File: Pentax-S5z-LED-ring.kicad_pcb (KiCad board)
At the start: 2 copper layers, 40 x 40 mm, 52 parts, among them IC1 ATTINY13-S, P1 CONN_2, P2 +, P3 -, P4 CONN_2, Q1 MOSFET_N, SW1 SW_PUSH, SW2 SW_PUSH

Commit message: Minute tweaks.
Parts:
- P2: value + -> A
- P3: value - -> B
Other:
- board text added: "A"
- board text added: "B"
- board text removed: "A+"
- board text removed: "B-"
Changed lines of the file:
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@@
-(kicad_pcb (version 3) (host pcbnew "(2013-05-08 BZR 4145)-testing")
+(kicad_pcb (version 3) (host pcbnew "(2013-09-20 BZR 4325)-product")
   (general
     (links 71)
     (no_connects 0)
-    (area 37.066667 44.422948 92.483333 85.577052)
+    (area 37.066667 44.949999 92.483333 85.050001)
     (thickness 1.6)
     (drawings 26)
@@
     (mod_text_size 1 1)
     (mod_text_width 0.2)
-    (pad_size 1.5 1.4)
+    (pad_size 1.5 1.2)
     (pad_drill 0)
     (pad_to_mask_clearance 0)
@@
     (visible_elements FFFFFF7F)
     (pcbplotparams
-      (layerselection 300974081)
+      (layerselection 284196865)
       (usegerberextensions true)
       (excludeedgelayer true)
-      (linewidth 152400)
+      (linewidth 0.150000)
       (plotframeref false)
       (viasonmask false)
@@
       (effects (font (size 1 1) (thickness 0.2)) (justify mirror))
     )
-    (fp_text value + (at -2.75 0) (layer B.SilkS)
+    (fp_text value A (at -2.35 0.05) (layer B.SilkS)
       (effects (font (size 1 1) (thickness 0.2)) (justify mirror))
     )
@@
       (effects (font (size 1 1) (thickness 0.2)) (justify mirror))
     )
-    (fp_text value - (at 2.5 0) (layer B.SilkS)
+    (fp_text value B (at 2.25 0.05) (layer B.SilkS)
       (effects (font (size 1 1) (thickness 0.2)) (justify mirror))
     )
@@
     (fp_line (start -3 1.85) (end -3 -1.85) (layer F.SilkS) (width 0.2))
     (fp_line (start -3 -1.85) (end 3 -1.85) (layer F.SilkS) (width 0.2))
-    (pad 1 smd rect (at -3.9 0 205) (size 1.5 1.4)
+    (pad 1 smd rect (at -3.9 0 205) (size 1.5 1.2)
       (layers F.Cu F.Mask)
       (net 7 N-0000011)
@@
     (fp_line (start -3 1.85) (end -3 -1.85) (layer F.SilkS) (width 0.2))
     (fp_line (start -3 -1.85) (end 3 -1.85) (layer F.SilkS) (width 0.2))
-    (pad 1 smd rect (at -3.9 0 335) (size 1.5 1.4)
+    (pad 1 smd rect (at -3.9 0 335) (size 1.5 1.2)
       (layers F.Cu F.Mask)
       (net 15 N-000002)
@@
     (effects (font (size 1 1) (thickness 0.2)))
   )
-  (gr_text B- (at 55.6 61.2 90) (layer F.SilkS)
+  (gr_text B (at 55.6 61.6 90) (layer F.SilkS)
     (effects (font (size 1 1) (thickness 0.2)))
   )
-  (gr_text A+ (at 55.6 68.7 90) (layer F.SilkS)
+  (gr_text A (at 55.6 68.4 90) (layer F.SilkS)
     (effects (font (size 1 1) (thickness 0.2)))
   )

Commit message: Added 3D modules for the PLCC2-3528 LEDs + silkscreen tweaks.
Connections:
- IC1 pad 2: N-000006 -> (no net)
- IC1 pad 3: N-000005 -> (no net)
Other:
- board text added: "+"

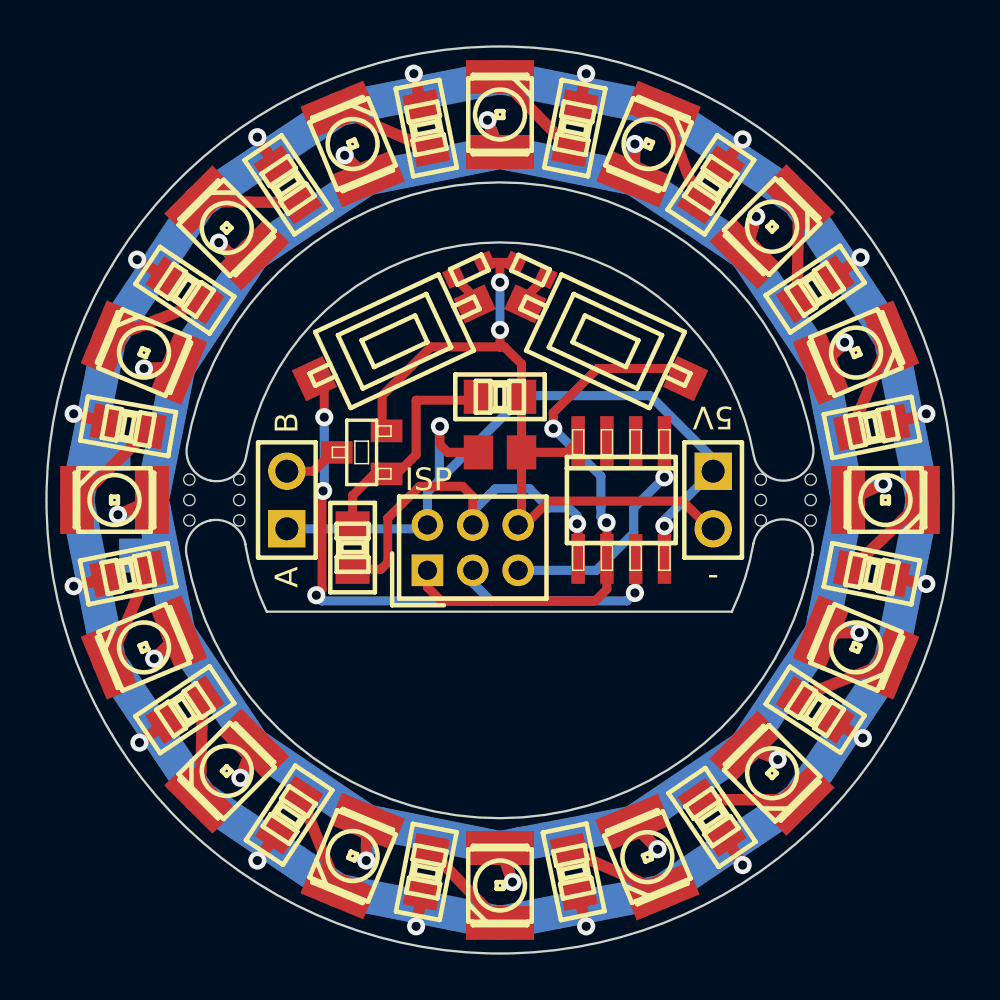
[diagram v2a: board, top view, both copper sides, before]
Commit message: Switched ATtiny13 to DFN10 package.
Had to move to KiCAD's new way of handling footprint libraries.
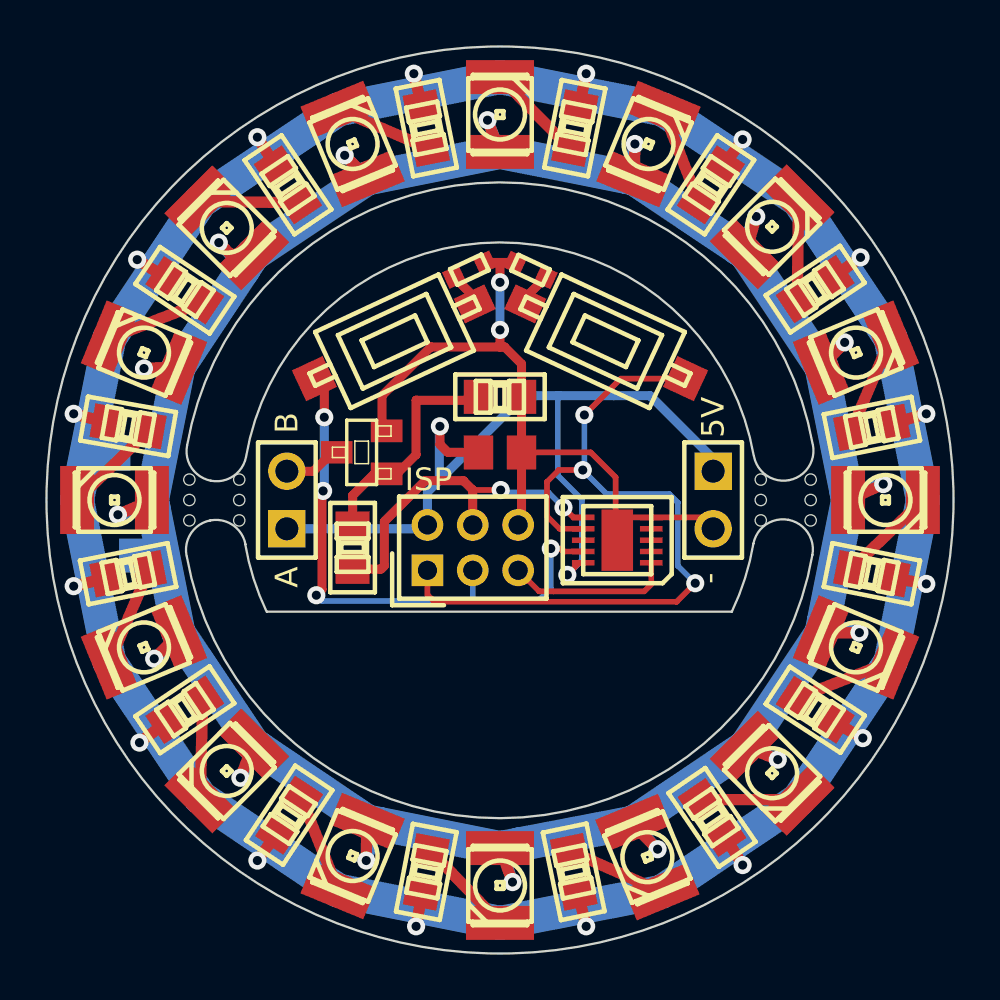
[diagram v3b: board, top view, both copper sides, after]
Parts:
- IC1: value ATTINY13-S -> MADW__ATTINY13-MM; footprint -SOIC8 -> my_parts:MADW__MLF10
- P2: value A -> +
- P3: value B -> -
- moved IC1 1.78 mm to (70.2, 66.8)
- moved G2 1.38 mm to (71.1, 63.1)
- moved G1 0.77 mm to (59.1, 63.2)
- renumbered G*** to G1, G*** to G1.1, G*** to G2, G*** to G2.1
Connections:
- IC1 pad 2: (no net) -> Net-(IC1-Pad2)
- IC1 pad 3: (no net) -> Net-(IC1-Pad3)
- IC1 pad 4: GND -> Net-(IC1-Pad4)
- IC1 pad 5: /PWM -> GND
- IC1 pad 6: /MISO -> /PWM
- IC1 pad 7: /SCK -> /MISO
- IC1 pad 8: +5V -> Net-(IC1-Pad8)
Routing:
- net /MISO: track 24.6 -> 34.8 mm, vias 2 -> 3
- net +5V: track 34.1 -> 38.9 mm
- net /RESET: track 10.4 -> 7.33 mm, vias 1 -> 0
- net /PWM: track 17.4 -> 15.1 mm, vias 1 -> 2
- net /SCK: track 27.4 -> 25.4 mm
- net Net-(D1-Pad1): track 152.8 -> 151.0 mm
- net GND: track 33.9 -> 35.1 mm
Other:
- net class Default: clearance 0.25 -> 0.2
- rule trace_clearance: 0.25 -> 0.2
- board text added: "V1.01.a"
- board text added: "V1.01.a 2013"
- board text removed: "+"
- board text removed: "V1.0"
- board text removed: "V1.0 2013"

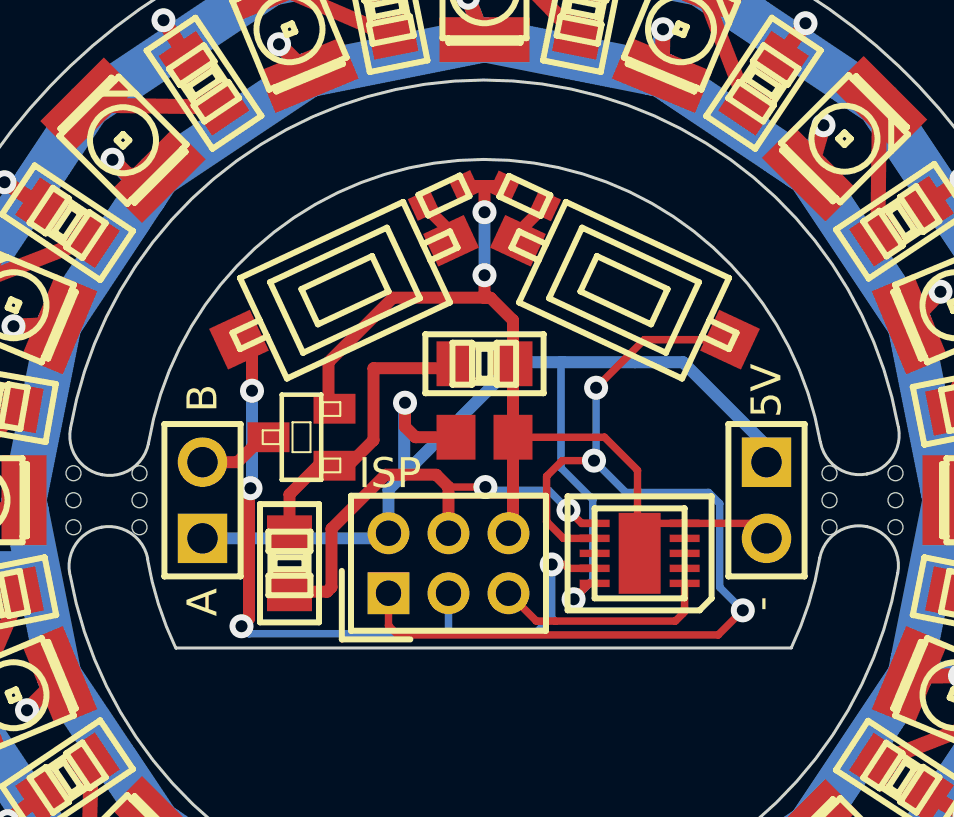
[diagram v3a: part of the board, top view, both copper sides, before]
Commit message: Shoved some traces around to stay clear of button switch bodies.
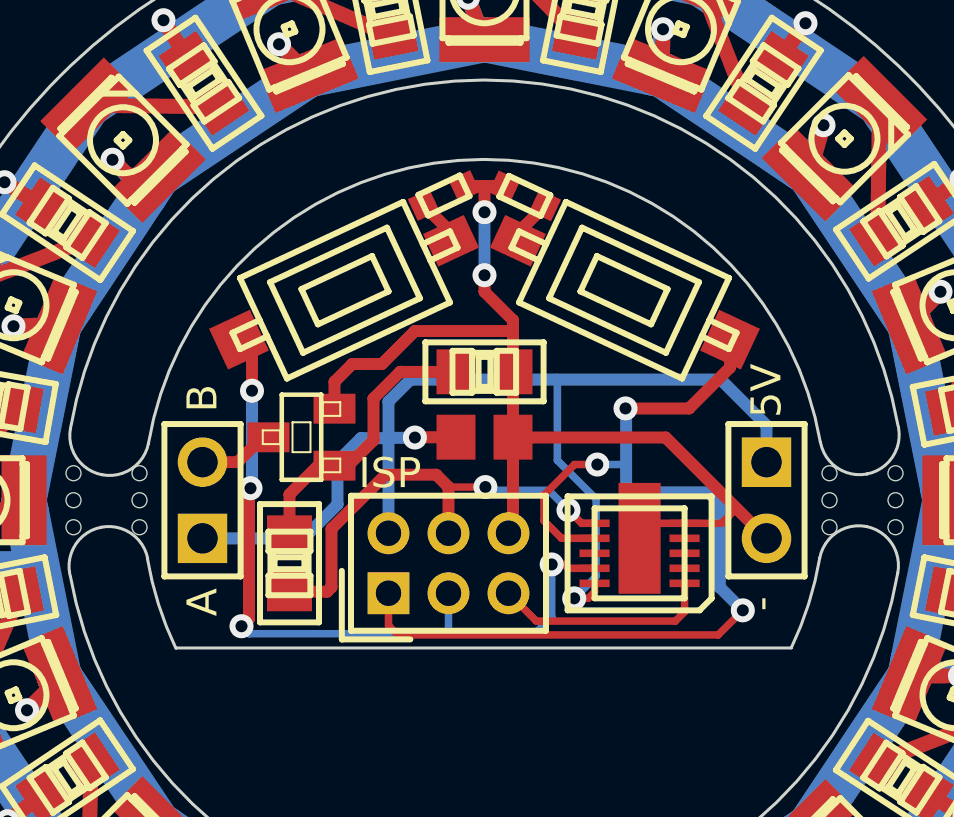
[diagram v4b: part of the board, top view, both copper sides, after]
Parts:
- moved R18 0.27 mm to (65.0, 60.7)
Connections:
- IC1 pad 2: Net-(IC1-Pad2) -> (no net)
- IC1 pad 3: Net-(IC1-Pad3) -> (no net)
- IC1 pad 4: Net-(IC1-Pad4) -> (no net)
- IC1 pad 8: Net-(IC1-Pad8) -> (no net)
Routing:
- net GND: track 35.1 -> 36.0 mm
- net Net-(Q1-Pad1): track 10.1 -> 9.40 mm

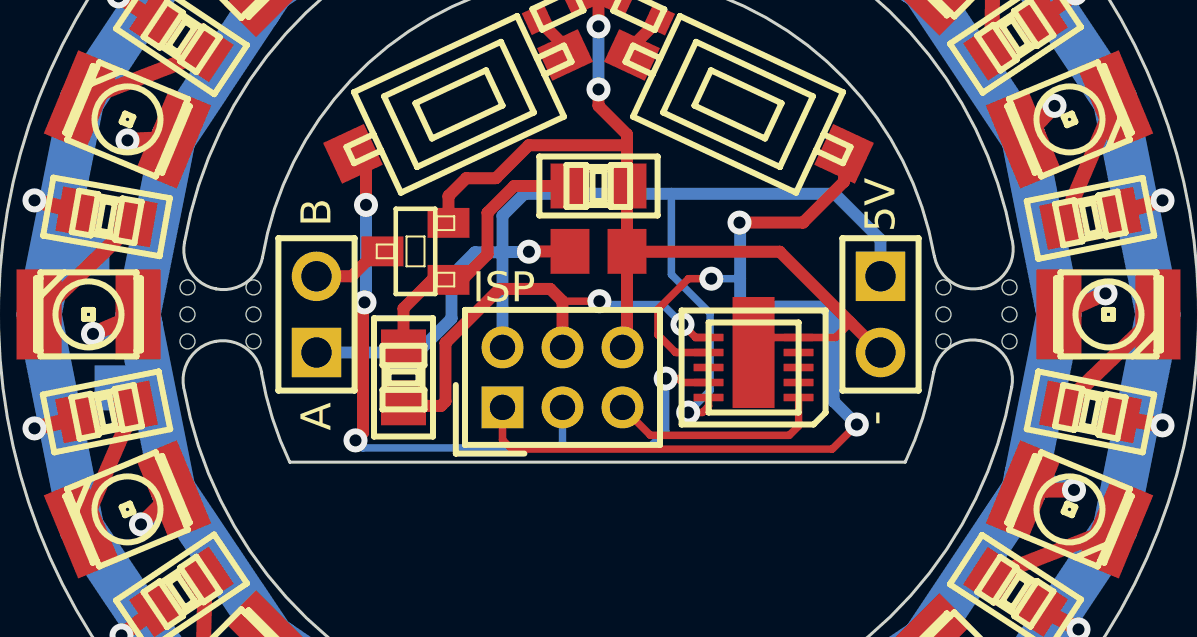
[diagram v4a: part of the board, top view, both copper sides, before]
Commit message: Replaced ISP-header with a pogo-pin compatible one (1.27mm pin-spacing).
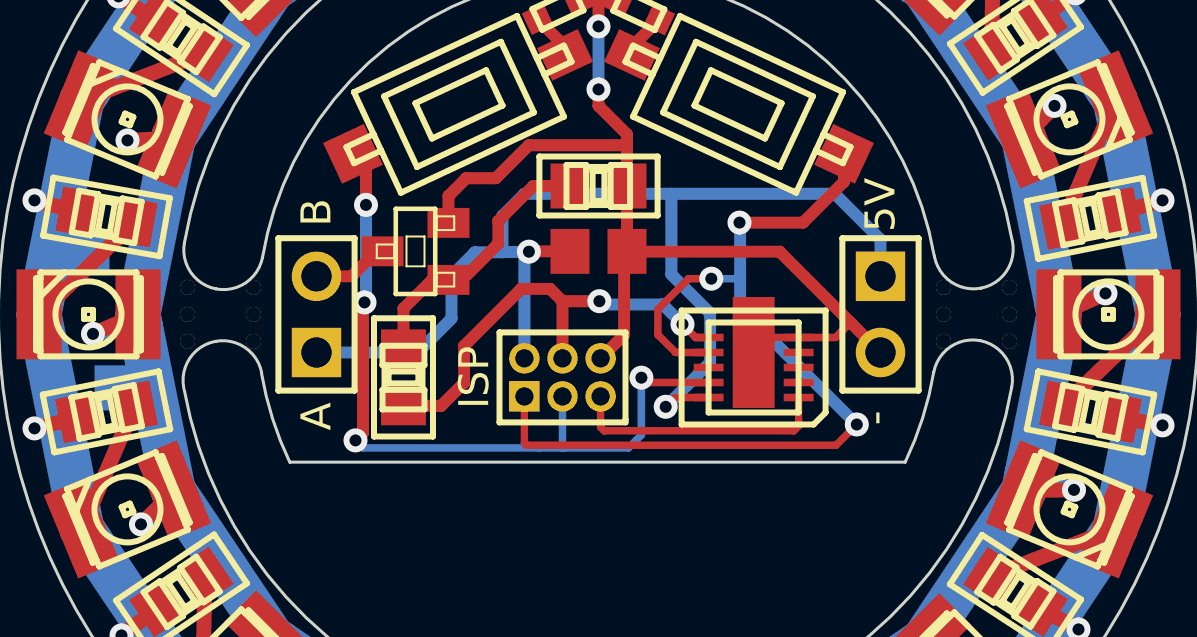
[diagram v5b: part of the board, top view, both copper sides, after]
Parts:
- JP1: footprint MADW__PIN_ARRAY_3x2_2mm -> my_parts:MADW__PIN_ARRAY_3x2_1.27mm
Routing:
- net /MISO: track 34.4 -> 32.3 mm
- net /RESET: track 7.33 -> 8.69 mm
- net +5V: track 39.1 -> 40.1 mm
- net GND: track 36.0 -> 36.6 mm
- net /SCK: track 25.2 -> 25.7 mm
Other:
- board text added: "V1.01.b"
- board text added: "V1.01.b 2013"
- board text removed: "V1.01.a"
- board text removed: "V1.01.a 2013"

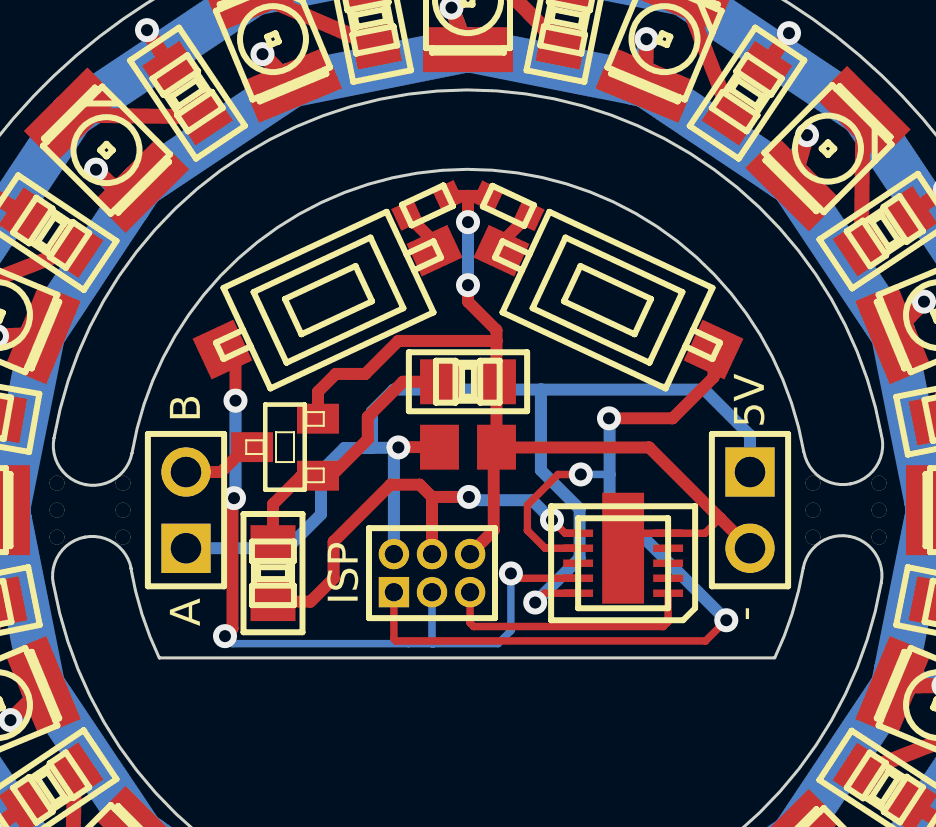
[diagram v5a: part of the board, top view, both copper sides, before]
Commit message: Shoved some parts around. Should be a bit easier to assemble.
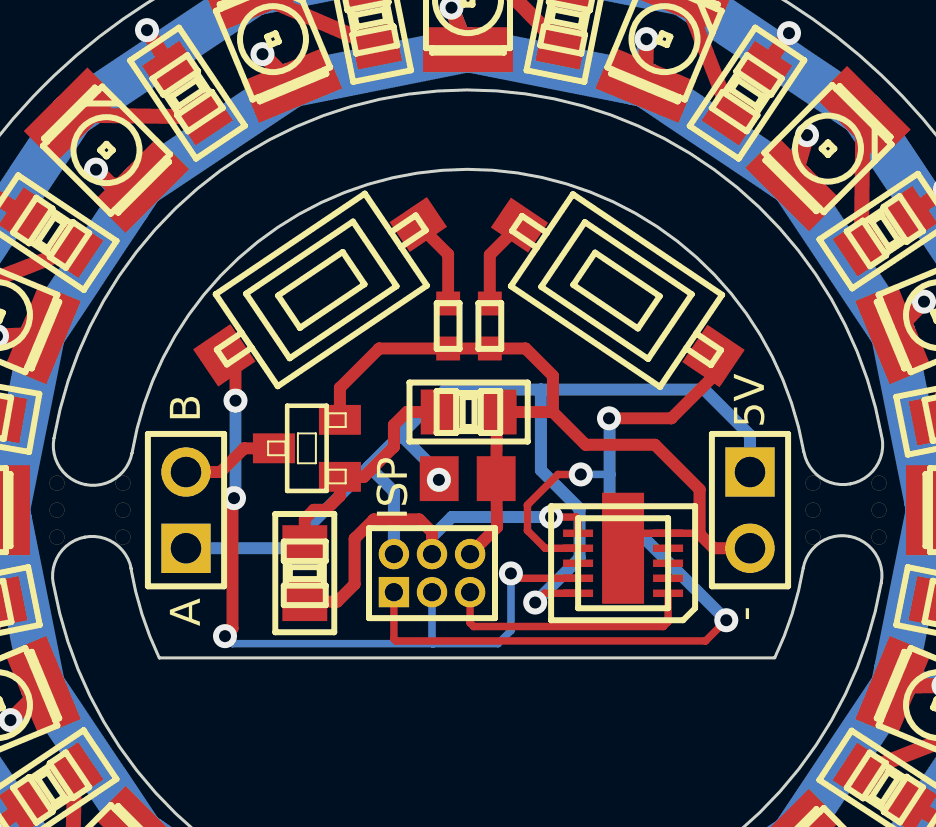
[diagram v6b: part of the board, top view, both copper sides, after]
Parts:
- moved R20 4.07 mm to (64.3, 58.9), turned to 270 degrees
- moved R19 4.06 mm to (65.7, 58.9), turned to 270 degrees
- moved R17 1.06 mm to (59.6, 67.1)
- moved C1 1.05 mm to (65.0, 64.0)
- moved R18 1.01 mm to (65.0, 61.7)
- moved Q1 0.73 mm to (59.6, 62.9)
- moved SW1 0.44 mm to (70.0, 57.7), turned to 326 degrees
- moved SW2 0.42 mm to (60.1, 57.7), turned to 214 degrees
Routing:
- net GND: track 36.6 -> 30.7 mm, vias 2 -> 0
- net +5V: track 40.1 -> 38.0 mm
- net /PWM: track 15.1 -> 13.4 mm, vias 2 -> 1
- net Net-(R20-Pad1): track 1.57 -> 3.05 mm
- net Net-(R19-Pad1): track 1.56 -> 3.02 mm
- net Net-(Q1-Pad1): track 9.03 -> 7.65 mm
- net Net-(P4-Pad2): track 2.34 -> 3.26 mm
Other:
- board text added: "V1.01.c"
- board text added: "V1.01.c 2013"
- board text removed: "V1.01.b"
- board text removed: "V1.01.b 2013"

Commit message: Layout tweaks.
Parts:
- C1: footprint MADW__C0805 -> my_parts:MADW__C0805
- moved R18 0.23 mm to (65.0, 61.5)
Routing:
- net /MISO: track 32.0 -> 31.0 mm
- net /SCK: track 25.5 -> 24.8 mm
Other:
- board text added: "+"
- board text added: "IN"
- board text added: "OUT"
- board text added: "V1.01.d"
- board text added: "V1.01.d 2013"
- board text removed: "V1.01.c"
- board text removed: "V1.01.c 2013"

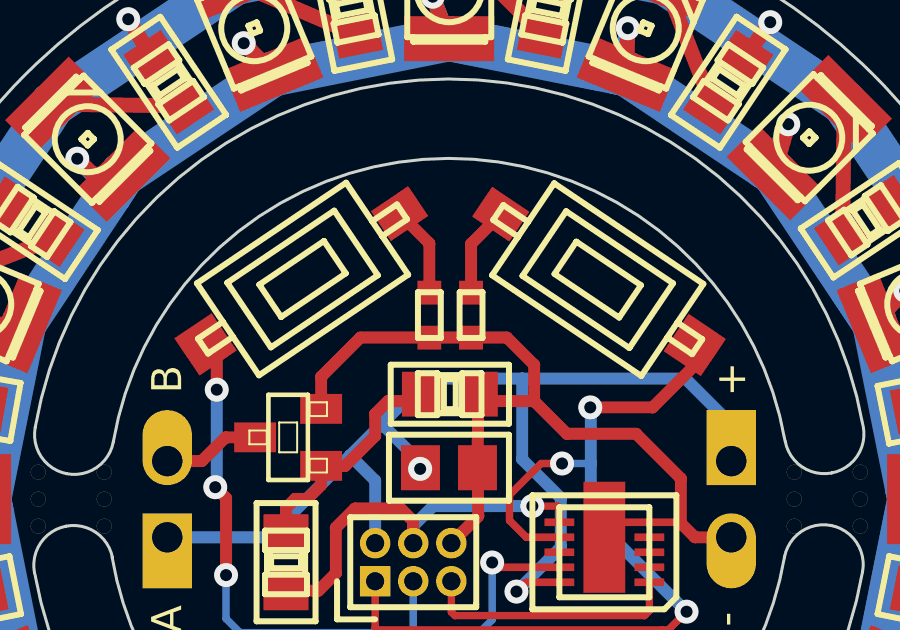
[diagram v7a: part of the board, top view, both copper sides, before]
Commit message: Changed 0603 footprint for pull-down resistors (a bit larger).
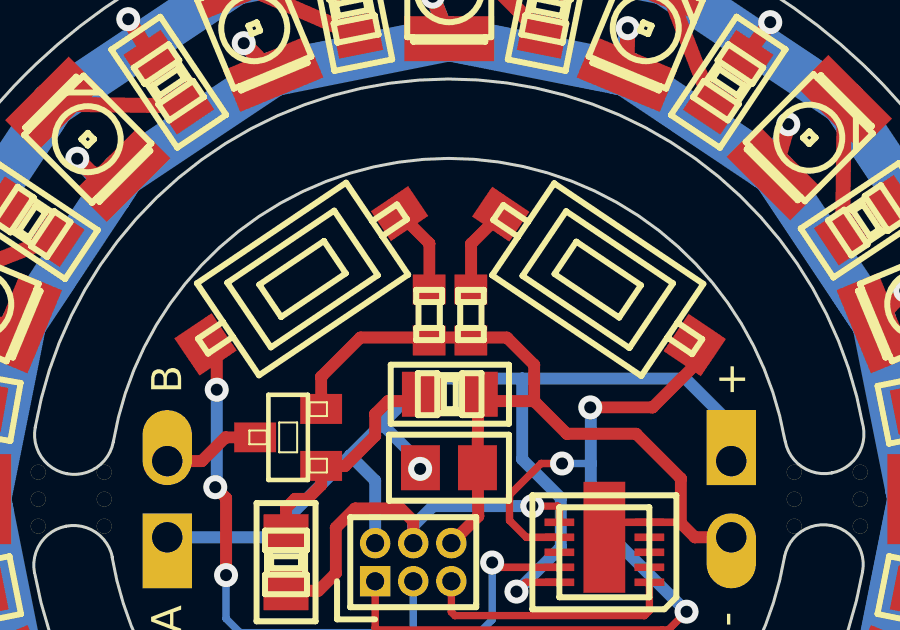
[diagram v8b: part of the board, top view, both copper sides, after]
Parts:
- R19, R20: footprint MADW__R0603 -> my_parts:MADW__R0603_2
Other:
- board text added: "2015"
- board text added: "V1.01.e"
- board text added: "V1.01.e 2015"
- board text removed: "2013"
- board text removed: "V1.01.d"
- board text removed: "V1.01.d 2013"
